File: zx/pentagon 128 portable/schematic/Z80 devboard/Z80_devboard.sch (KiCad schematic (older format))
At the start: 38 parts, among them IC1 Z84C0020AEG, IC2 TXB0108PWR, IC3 TXB0108PWR, IC4 TXB0108PWR, IC5 TXB0108PWR, IC6 TXB0108PWR, J1 Conn_01x08, J2 Conn_01x16, J3 Conn_01x11, J4 Conn_01x02, J5 Conn_01x03, J6 Conn_01x03, J7 Conn_01x03, U1 LD1117S50TR_SOT223, U2 LD1117S33TR_SOT223

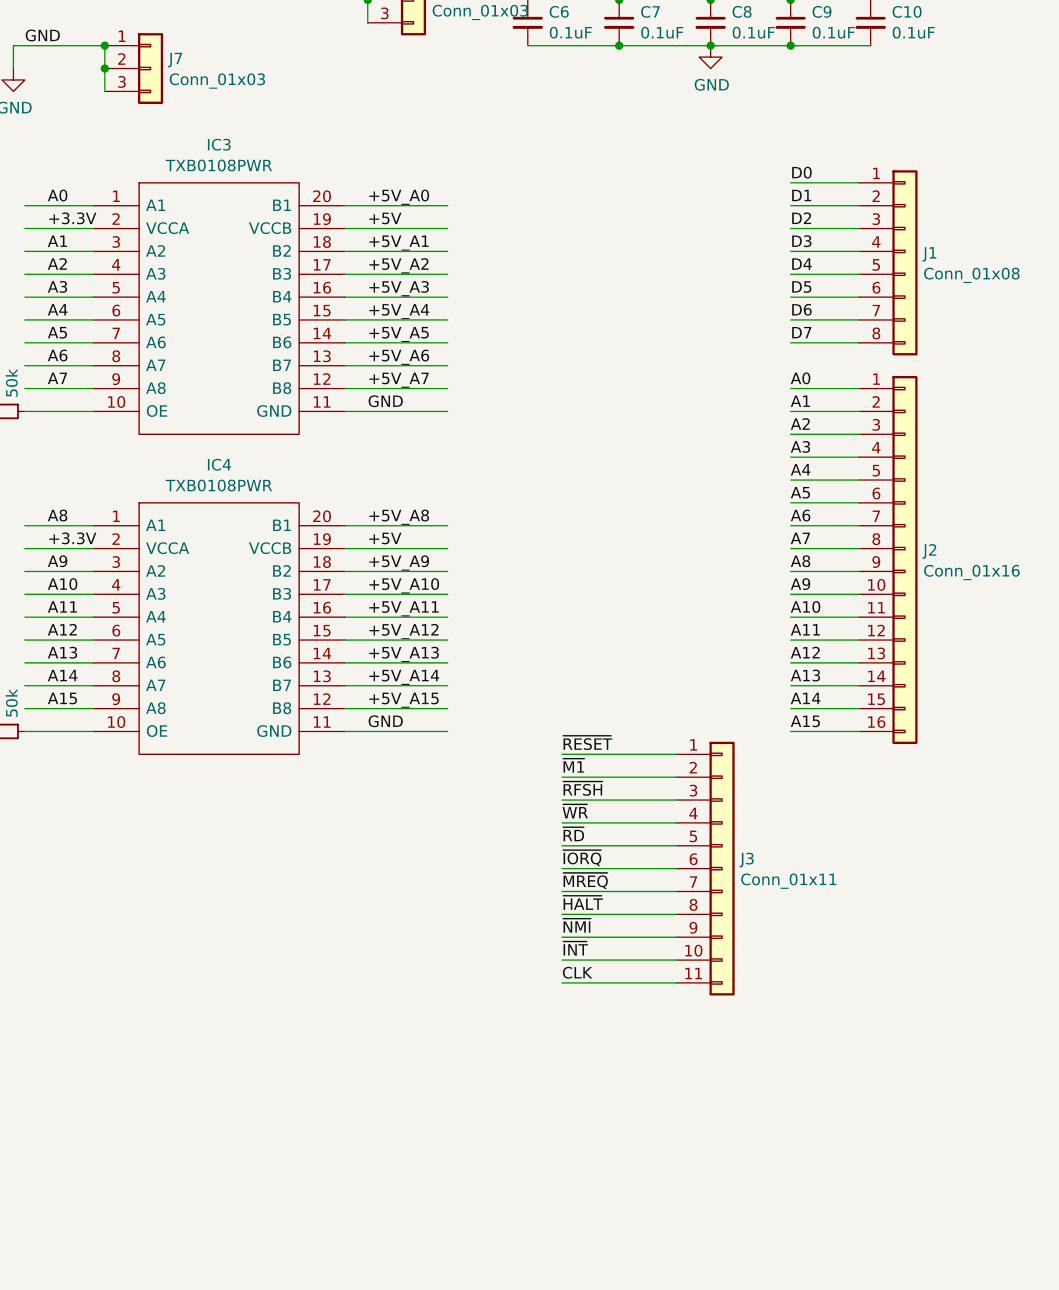
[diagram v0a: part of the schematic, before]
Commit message: reorganizing. finished ram and keyboard, updated z80
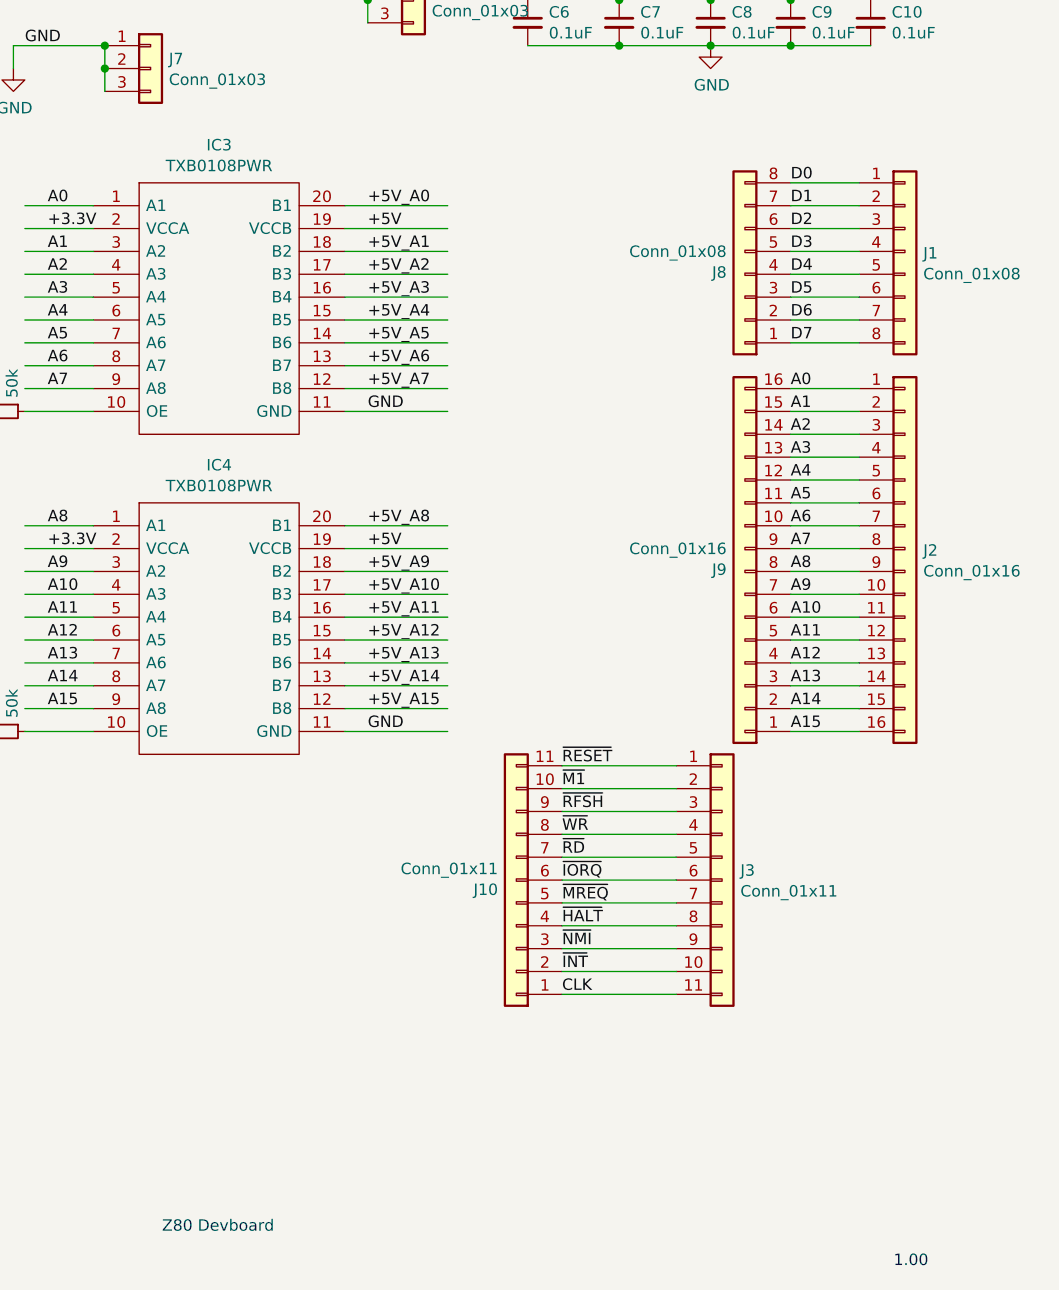
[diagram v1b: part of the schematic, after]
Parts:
- added J10: Conn_01x11, Connector_PinHeader_2.54mm:PinHeader_1x11_P2.54mm_Vertical, symbol Connector_Generic:Conn_01x11
- added J8: Conn_01x08, Connector_PinHeader_2.54mm:PinHeader_1x08_P2.54mm_Vertical, symbol Connector_Generic:Conn_01x08
- added J9: Conn_01x16, Connector_PinHeader_2.54mm:PinHeader_1x16_P2.54mm_Vertical, symbol Connector_Generic:Conn_01x16
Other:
- note added: "1.00"
- note added: "Z80 Devboard"
- moved on the sheet: J3
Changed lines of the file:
@@
 L Connector_Generic:Conn_01x11 J3
 U 1 1 5FA988C2
-P 9850 5900
-F 0 "J3" H 9930 5942 50  0000 L CNN
-F 1 "Conn_01x11" H 9930 5851 50  0000 L CNN
-F 2 "Connector_PinHeader_2.54mm:PinHeader_1x11_P2.54mm_Vertical" H 9850 5900 50  0001 C CNN
-F 3 "~" H 9850 5900 50  0001 C CNN
-	1    9850 5900
-	1    0    0    -1
-$EndComp
-Text Label 9150 5600 0    50   ~ 0
+P 9850 5950
+F 0 "J3" H 9930 5992 50  0000 L CNN
+F 1 "Conn_01x11" H 9930 5901 50  0000 L CNN
+F 2 "Connector_PinHeader_2.54mm:PinHeader_1x11_P2.54mm_Vertical" H 9850 5950 50  0001 C CNN
+F 3 "~" H 9850 5950 50  0001 C CNN
+	1    9850 5950
+	1    0    0    -1
+$EndComp
+Text Label 9150 5650 0    50   ~ 0
 ~RFSH
 Wire Wire Line
-	9650 5400 9150 5400
-Wire Wire Line
-	9650 5500 9150 5500
-Wire Wire Line
-	9650 5600 9150 5600
-Wire Wire Line
-	9650 5700 9150 5700
-Wire Wire Line
-	9650 5800 9150 5800
-Wire Wire Line
-	9650 5900 9150 5900
-Wire Wire Line
-	9650 6000 9150 6000
-Wire Wire Line
-	9650 6100 9150 6100
-Wire Wire Line
-	9650 6200 9150 6200
-Wire Wire Line
-	9650 6300 9150 6300
-Wire Wire Line
-	9650 6400 9150 6400
-Text Label 9150 5500 0    50   ~ 0
+	9650 5450 9150 5450
+Wire Wire Line
+	9650 5550 9150 5550
+Wire Wire Line
+	9650 5650 9150 5650
+Wire Wire Line
+	9650 5750 9150 5750
+Wire Wire Line
+	9650 5850 9150 5850
+Wire Wire Line
+	9650 5950 9150 5950
+Wire Wire Line
+	9650 6050 9150 6050
+Wire Wire Line
+	9650 6150 9150 6150
+Wire Wire Line
+	9650 6250 9150 6250
+Wire Wire Line
+	9650 6350 9150 6350
+Wire Wire Line
+	9650 6450 9150 6450
+Text Label 9150 5550 0    50   ~ 0
 ~M1
-Text Label 9150 5400 0    50   ~ 0
+Text Label 9150 5450 0    50   ~ 0
 ~RESET
-Text Label 9150 6300 0    50   ~ 0
+Text Label 9150 6350 0    50   ~ 0
 ~INT
-Text Label 9150 6200 0    50   ~ 0
+Text Label 9150 6250 0    50   ~ 0
 ~NMI
-Text Label 9150 6100 0    50   ~ 0
+Text Label 9150 6150 0    50   ~ 0
 ~HALT
-Text Label 9150 6000 0    50   ~ 0
+Text Label 9150 6050 0    50   ~ 0
 ~MREQ
-Text Label 9150 5900 0    50   ~ 0
+Text Label 9150 5950 0    50   ~ 0
 ~IORQ
-Text Label 9150 5800 0    50   ~ 0
+Text Label 9150 5850 0    50   ~ 0
 ~RD
-Text Label 9150 5700 0    50   ~ 0
+Text Label 9150 5750 0    50   ~ 0
 ~WR
-Text Label 9150 6400 0    50   ~ 0
+Text Label 9150 6450 0    50   ~ 0
 CLK
 $Comp
@@
 Wire Wire Line
 	1350 3800 1000 3800
+$Comp
+L Connector_Generic:Conn_01x08 J8
+U 1 1 5F67168B
+P 9950 3300
+F 0 "J8" H 10030 3292 50  0000 L CNN
+F 1 "Conn_01x08" H 10030 3201 50  0000 L CNN
+F 2 "Connector_PinHeader_2.54mm:PinHeader_1x08_P2.54mm_Vertical" H 9950 3300 50  0001 C CNN
+F 3 "~" H 9950 3300 50  0001 C CNN
+	1    9950 3300
+	-1   0    0    1
+$EndComp
+$Comp
+L Connector_Generic:Conn_01x16 J9
+U 1 1 5F672E66
+P 9950 4600
+F 0 "J9" H 10030 4592 50  0000 L CNN
+F 1 "Conn_01x16" H 10030 4501 50  0000 L CNN
+F 2 "Connector_PinHeader_2.54mm:PinHeader_1x16_P2.54mm_Vertical" H 9950 4600 50  0001 C CNN
+F 3 "~" H 9950 4600 50  0001 C CNN
+	1    9950 4600
+	-1   0    0    1
+$EndComp
+$Comp
+L Connector_Generic:Conn_01x11 J10
+U 1 1 5F688725
+P 8950 5950
+F 0 "J10" H 9030 5992 50  0000 L CNN
+F 1 "Conn_01x11" H 9030 5901 50  0000 L CNN
+F 2 "Connector_PinHeader_2.54mm:PinHeader_1x11_P2.54mm_Vertical" H 8950 5950 50  0001 C CNN
+F 3 "~" H 8950 5950 50  0001 C CNN
+	1    8950 5950
+	-1   0    0    1
+$EndComp
+Text Notes 10600 7650 0    50   ~ 0
+1.00
+Text Notes 7400 7500 0    50   ~ 0
+Z80 Devboard
 $EndSCHEMATC
